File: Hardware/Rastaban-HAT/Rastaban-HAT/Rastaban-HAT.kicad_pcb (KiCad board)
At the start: 2 copper layers, 99.1 x 99.7 mm, 129 parts, among them IC1 BCR420UW6-7, IC2 BCM53DS, J1 1778780, J10 GPIO, J11 Conn_01x06_Male, J12 Conn_01x03_Male, J13 Conn_01x03_Male, J2 1778780, J3 1778780, J4 Screw_Terminal_01x02, J5 Jack-DC 12V+, J6 SM04B-SRSS-TB(LF)(SN), J7 Screw_Terminal_01x02, J8 Screw_Terminal_01x02, J9 Conn_01x05_Male, M1 Fan, Q1 PMV15ENE, Q2 PMV15ENE, Q3 DMG2305UX-7, Q4 PMV15ENE, Q5 PMV15ENE, Q6 2N70002HWX, U1 DRV8870DDA, U10 xl6009_module, U2 TLV1117-33, U3 TMC2208_Carrier, U4 TMC2208_Carrier, U5 RT7272AGSP, U6 TMC2208_Carrier, U7 DRV8838 POLOLU, U8 TLV1117-33, U9 CAT24C256

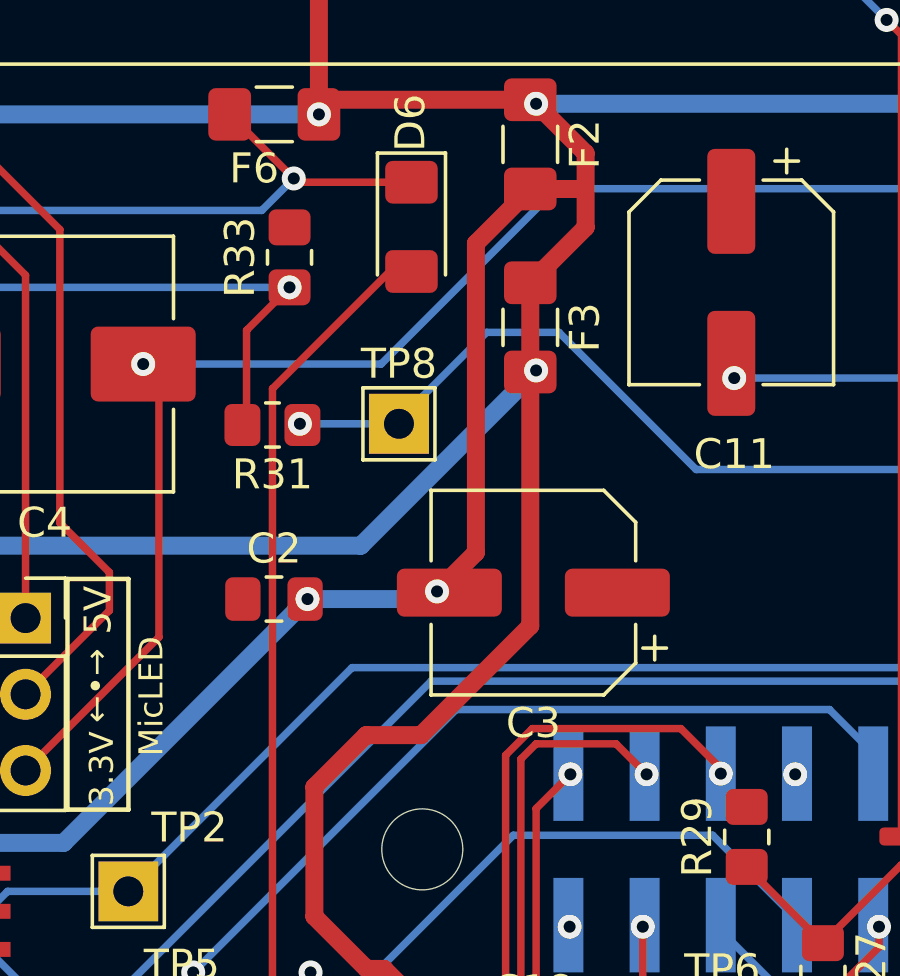
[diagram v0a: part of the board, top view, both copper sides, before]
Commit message: fixed parity problem ERC: 0 err 0 war
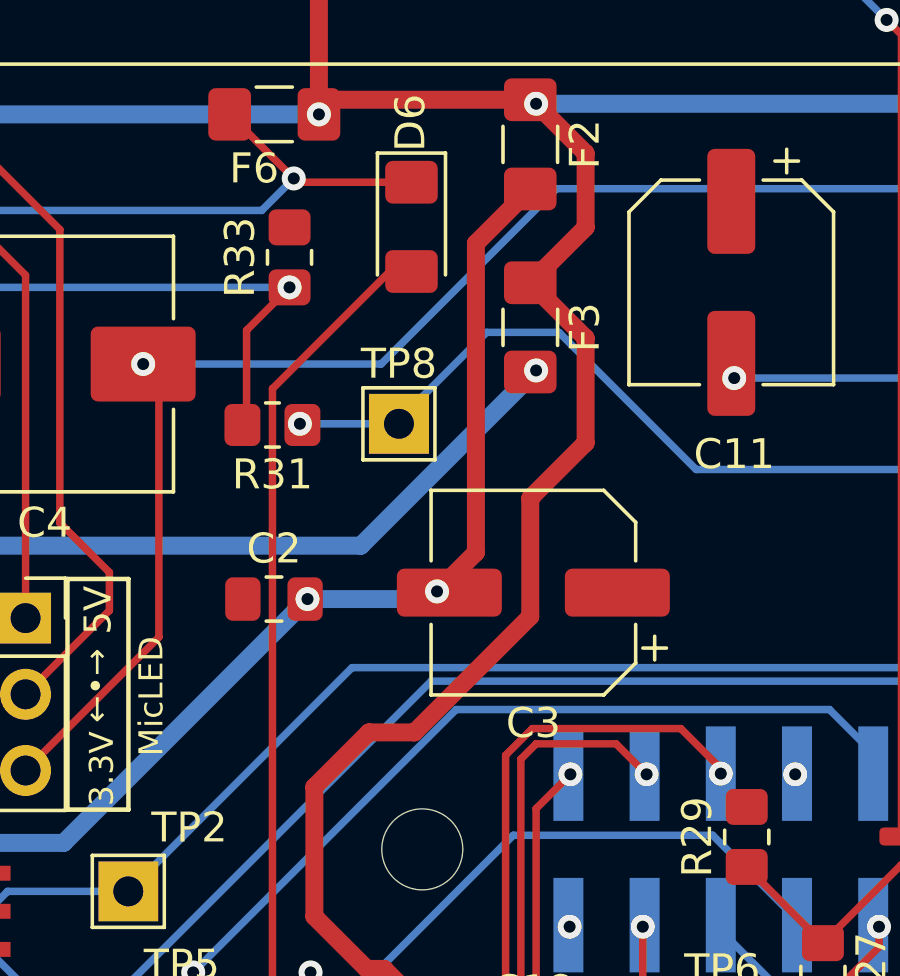
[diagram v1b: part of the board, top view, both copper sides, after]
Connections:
- C18 pad 1: Net-(C2-Pad2) -> 12V+
- C6 pad 1: Net-(C2-Pad2) -> 12V+
- C7 pad 1: Net-(C2-Pad2) -> 12V+
- C8 pad 1: Net-(C2-Pad2) -> 12V+
- F1 pad 1: Net-(C2-Pad2) -> 12V+
- F2 pad 1: Net-(C2-Pad2) -> 12V+
- F3 pad 1: Net-(C2-Pad2) -> 12V+
- F3 pad 2: Net-(C2-Pad2) -> Net-(F3-Pad2)
- F5 pad 1: Net-(C2-Pad2) -> 12V+
- F6 pad 1: Net-(C2-Pad2) -> 12V+
- FB1 pad 2: Net-(C2-Pad2) -> 12V+
- JP2 pad 3: Net-(C2-Pad2) -> 12V+
- JP3 pad 3: Net-(C2-Pad2) -> 12V+
- R10 pad 1: Net-(C2-Pad2) -> 12V+
- R3 pad 2: Net-(C2-Pad2) -> Net-(F3-Pad2)
- U10 pad 1: Net-(C2-Pad2) -> 12V+
- U5 pad 8: Net-(C2-Pad2) -> 12V+
- U6 pad JP2_1: Net-(C2-Pad2) -> 12V+
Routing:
- net Net-(C2-Pad2): track 324.9 -> 39.6 mm, vias 14 -> 3
- net 12V+: track 0.00 -> 251.4 mm, vias 0 -> 9
- net Net-(F3-Pad2): track 0.00 -> 33.4 mm, vias 0 -> 2

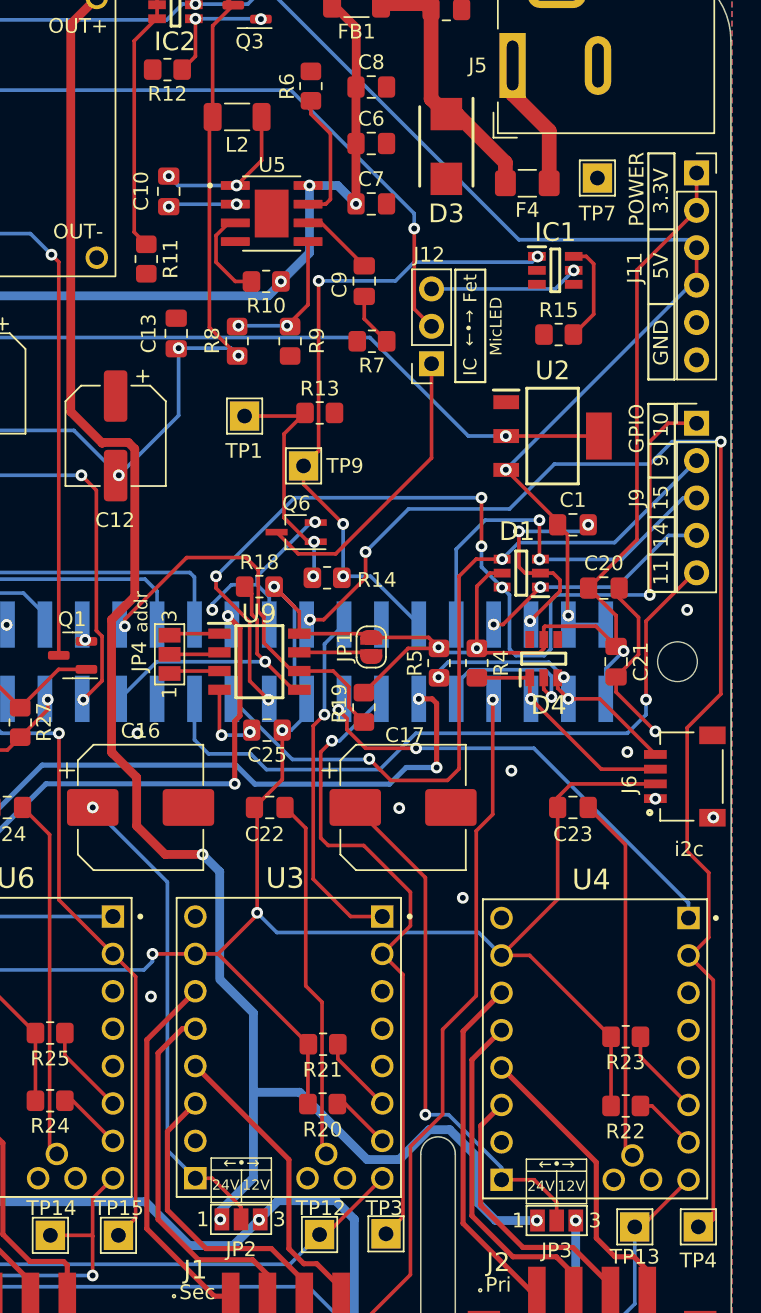
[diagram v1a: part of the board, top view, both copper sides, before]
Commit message: increased width stepper trace and rerun drc 0,0
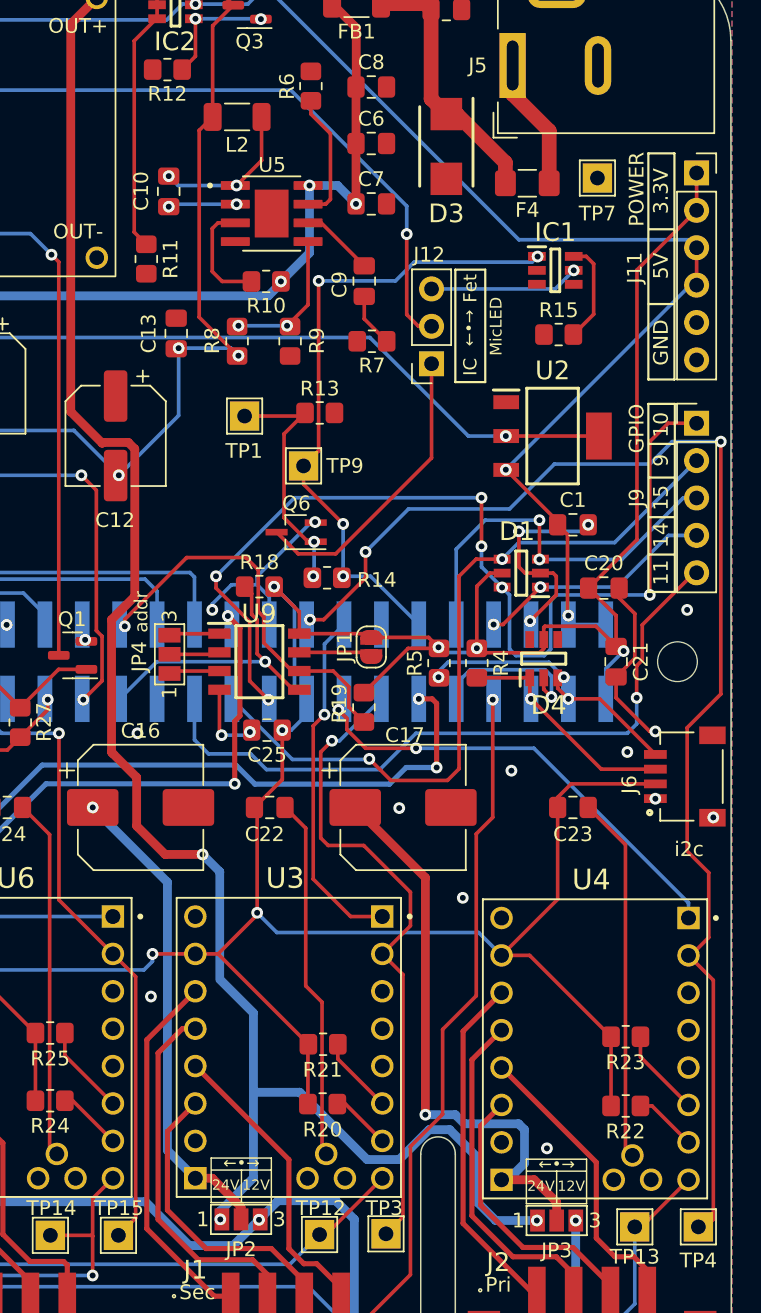
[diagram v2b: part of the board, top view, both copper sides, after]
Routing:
- net Net-(C17-Pad1): track 35.9 -> 39.9 mm
- net Net-(R10-Pad2): track 6.43 -> 7.59 mm
- net Net-(C11-Pad2): track 53.8 -> 54.4 mm
- net Net-(D2-PadK): track 79.2 -> 79.7 mm
- net GND: track 55.4 -> 55.2 mm, vias 24 -> 25

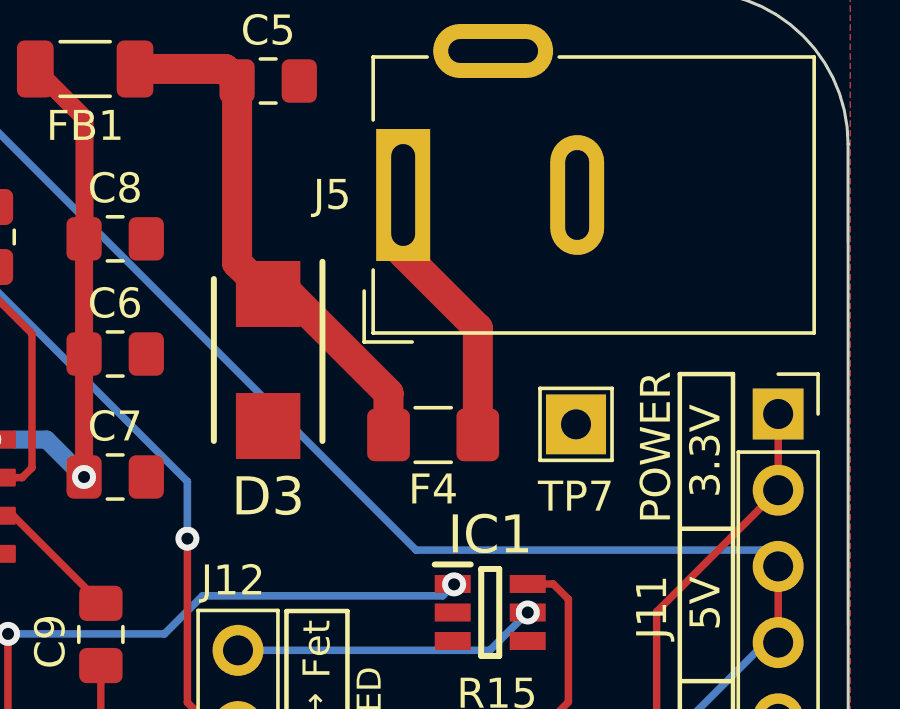
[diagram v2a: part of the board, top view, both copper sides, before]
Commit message: removed useless testpoint (GND)
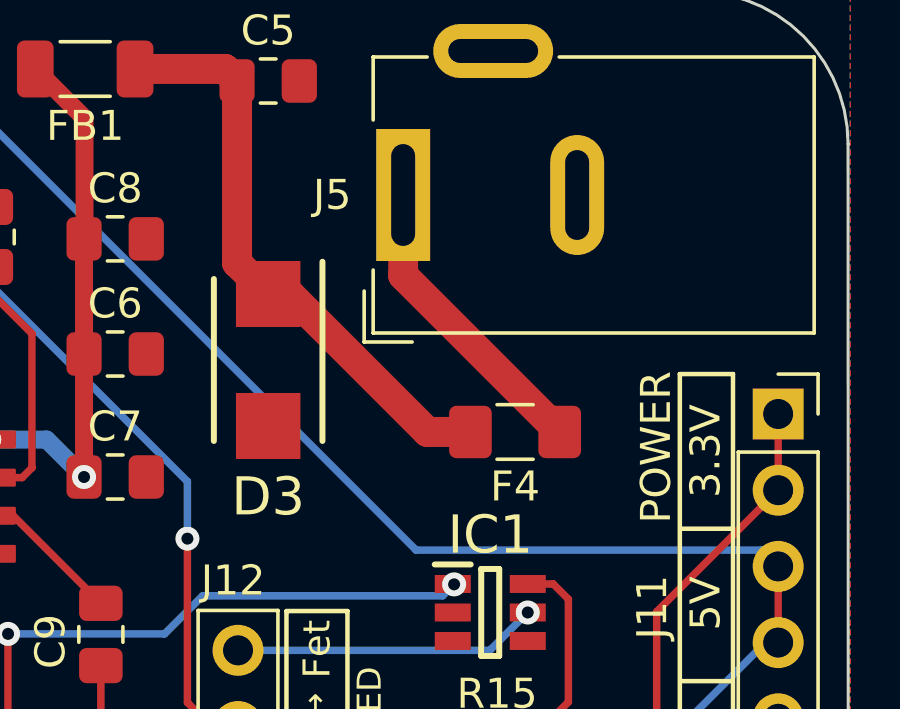
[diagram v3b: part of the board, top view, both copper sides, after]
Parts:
- removed TP7: TestPoint, TestPoint:TestPoint_THTPad_2.0x2.0mm_Drill1.0mm
- moved F4 2.73 mm to (240.5, 125.9)
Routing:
- net Net-(C5-Pad1): track 17.9 -> 19.7 mm
- net 12VIN: track 9.03 -> 10.1 mm
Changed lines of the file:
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@@
   )
   (footprint "Fuse:Fuse_1206_3216Metric_Pad1.42x1.75mm_HandSolder" (layer "F.Cu")
-    (at 237.808 125.958 180)
+    (at 240.538 125.857 180)
     (descr "Fuse SMD 1206 (3216 Metric), square (rectangular) end terminal, IPC_7351 nominal with elongated pad for handsoldering. (Body size source: http://www.tortai-tech.com/upload/download/2011102023233369053.pdf), generated with kicad-footprint-generator")
     (tags "fuse handsolder")
@@
     )
   )
-  (footprint "TestPoint:TestPoint_THTPad_2.0x2.0mm_Drill1.0mm" (layer "F.Cu")
-    (at 242.57 125.603)
-    (descr "THT rectangular pad as test Point, square 2.0mm_Drill1.0mm  side length, hole diameter 1.0mm")
-    (tags "test point THT pad rectangle square")
-    (property "LCSC" "x")
-    (property "Mouser" "x")
-    (property "Sheetfile" "Rastaban-HAT.kicad_sch")
-    (property "Sheetname" "")
-    (attr exclude_from_pos_files)
-    (fp_text reference "TP7" (at 0 2.413) (layer "F.SilkS")
-      (effects (font (size 1 1) (thickness 0.15)))
-    )
-    (fp_text value "TestPoint" (at 0 3.048) (layer "F.Fab")
-      (effects (font (size 1 1) (thickness 0.15)))
-    )
-    (fp_text user "${REFERENCE}" (at 0 -2) (layer "F.Fab")
-      (effects (font (size 1 1) (thickness 0.15)))
-    )
-    (fp_line (start 1.2 1.2) (end -1.2 1.2) (layer "F.SilkS") (width 0.12))
-    (fp_line (start 1.2 -1.2) (end 1.2 1.2) (layer "F.SilkS") (width 0.12))
-    (fp_line (start -1.2 -1.2) (end 1.2 -1.2) (layer "F.SilkS") (width 0.12))
-    (fp_line (start -1.2 1.2) (end -1.2 -1.2) (layer "F.SilkS") (width 0.12))
-    (fp_line (start -1.5 -1.5) (end -1.5 1.5) (layer "F.CrtYd") (width 0.05))
-    (fp_line (start -1.5 -1.5) (end 1.5 -1.5) (layer "F.CrtYd") (width 0.05))
-    (fp_line (start 1.5 1.5) (end -1.5 1.5) (layer "F.CrtYd") (width 0.05))
-    (fp_line (start 1.5 1.5) (end 1.5 -1.5) (layer "F.CrtYd") (width 0.05))
-    (pad "1" thru_hole rect (at 0 0) (size 2 2) (drill 1) (layers *.Cu *.Mask)
-      (net 1 "GND") (pinfunction "1") (pintype "passive"))
-  )
   (footprint "Package_TO_SOT_SMD:SOT-23" (layer "F.Cu")
     (at 167.308 167.458 90)
@@
   (segment (start 170.307 158.242) (end 178.054 158.242) (width 0.6) (layer "B.Cu") (net 3))
   (segment (start 227.8719 113.7566) (end 230.8691 113.7566) (width 1) (layer "F.Cu") (net 4))
+  (segment (start 232.308 121.258) (end 233.018 121.258) (width 1) (layer "F.Cu") (net 4))
   (segment (start 231.2705 114.158) (end 231.2705 120.2205) (width 1) (layer "F.Cu") (net 4))
   (segment (start 230.8691 113.7566) (end 231.2705 114.158) (width 1) (layer "F.Cu") (net 4))
-  (segment (start 232.308 121.258) (end 233.018 121.258) (width 1) (layer "F.Cu") (net 4))
-  (segment (start 236.3205 124.5605) (end 236.3205 125.958) (width 1) (layer "F.Cu") (net 4))
+  (segment (start 237.617 125.857) (end 239.0505 125.857) (width 1) (layer "F.Cu") (net 4))
+  (segment (start 233.018 121.258) (end 237.617 125.857) (width 1) (layer "F.Cu") (net 4))
   (segment (start 231.2705 120.2205) (end 232.308 121.258) (width 1) (layer "F.Cu") (net 4))
-  (segment (start 233.018 121.258) (end 236.3205 124.5605) (width 1) (layer "F.Cu") (net 4))
   (segment (start 227.8705 113.758) (end 227.8719 113.7566) (width 1) (layer "F.Cu") (net 4))
   (segment (start 226.731 135.168) (end 228.255 136.692) (width 0.25) (layer "F.Cu") (net 5))
@@
   (segment (start 167.6765 133.3865) (end 167.6765 134.366) (width 0.25) (layer "F.Cu") (net 11))
   (segment (start 162.376 131.507333) (end 165.797333 131.507333) (width 0.25) (layer "F.Cu") (net 11))
-  (segment (start 239.2955 122.3947) (end 236.808 119.9072) (width 1) (layer "F.Cu") (net 12))
-  (segment (start 236.808 119.9072) (end 236.808 117.958) (width 1) (layer "F.Cu") (net 12))
-  (segment (start 239.2955 125.958) (end 239.2955 122.3947) (width 1) (layer "F.Cu") (net 12))
+  (segment (start 242.0255 125.857) (end 236.808 120.6395) (width 1) (layer "F.Cu") (net 12))
+  (segment (start 236.808 120.6395) (end 236.808 117.958) (width 1) (layer "F.Cu") (net 12))
   (segment (start 240.598 160.983) (end 242.733 160.983) (width 0.25) (layer "F.Cu") (net 13))
   (segment (start 239.873 160.258) (end 240.598 160.983) (width 0.25) (layer "F.Cu") (net 13))

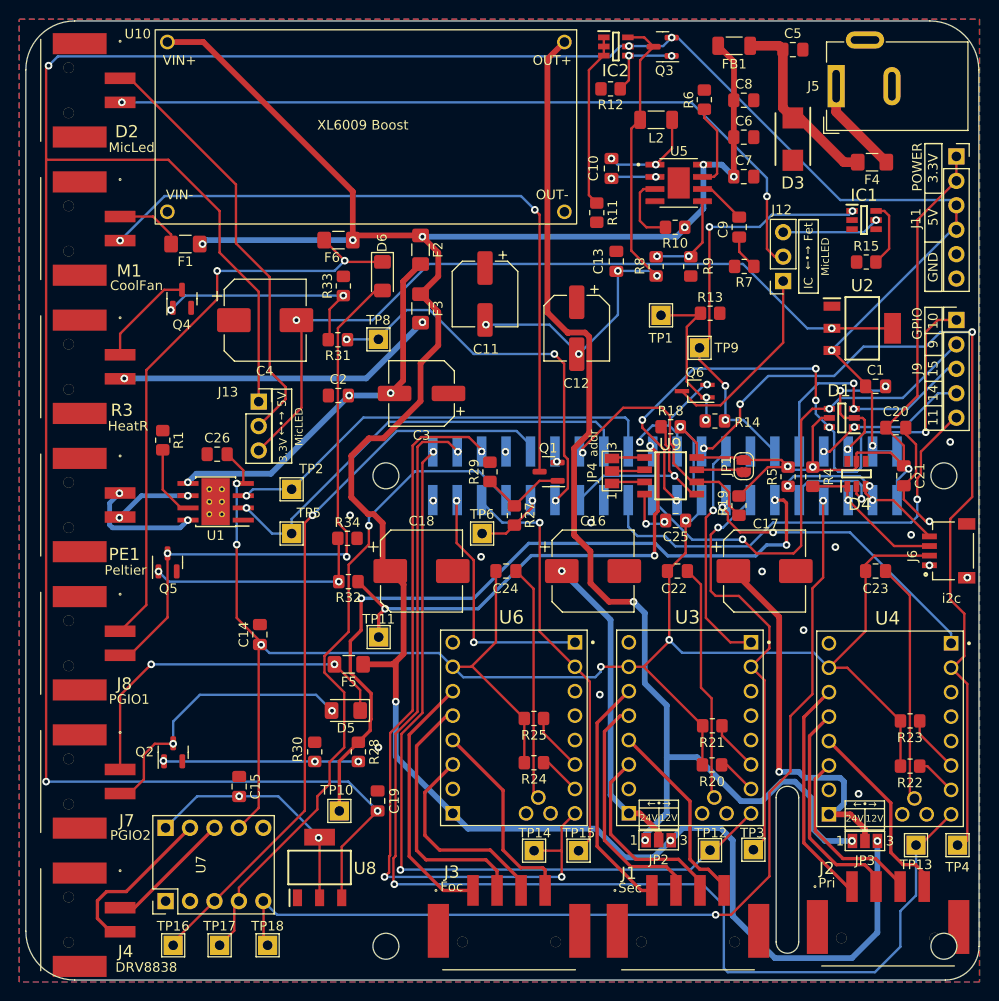
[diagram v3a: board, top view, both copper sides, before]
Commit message: improved wiring
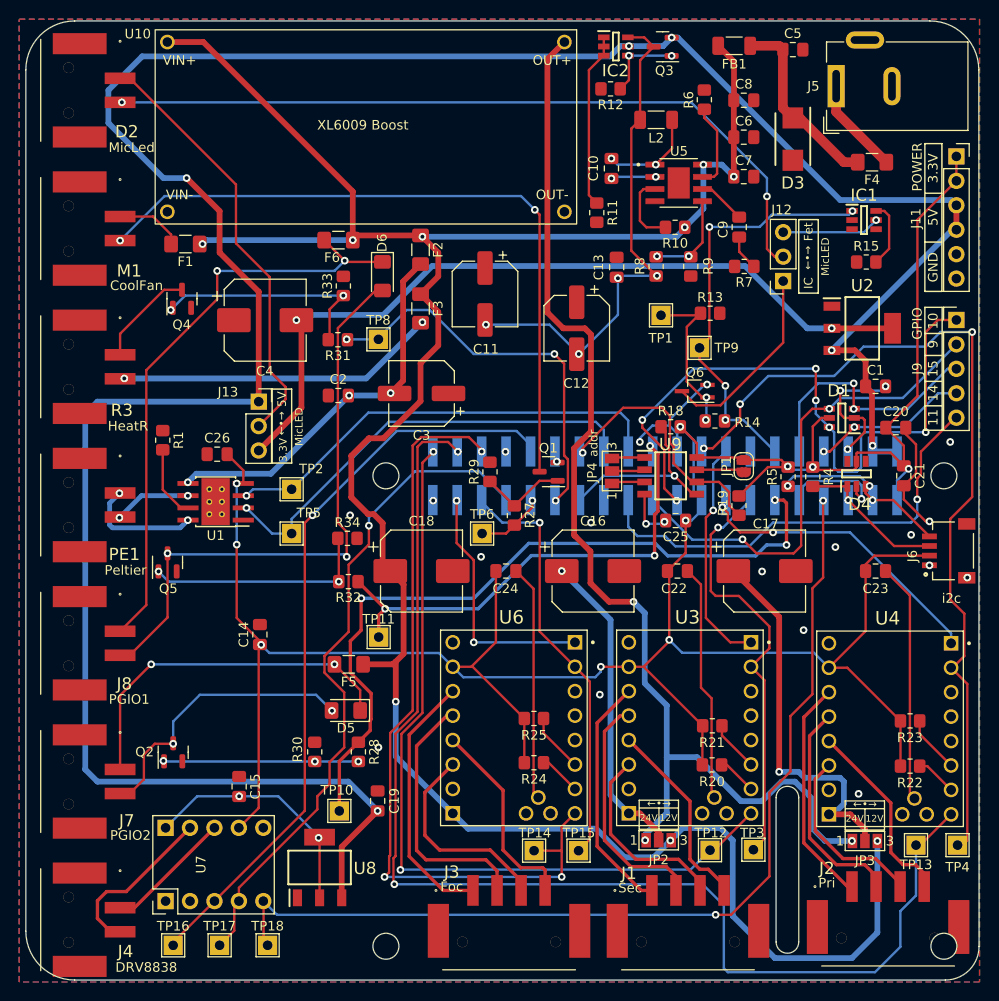
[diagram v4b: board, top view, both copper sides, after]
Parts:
- moved C13 0.62 mm to (214.0, 136.8)
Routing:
- net 5V+: track 300.3 -> 272.5 mm, vias 7 -> 6
- net Net-(C11-Pad2): track 54.4 -> 53.5 mm

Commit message: added silkscreen on back
added useful board information
added logo to files
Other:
- board text added: "Project: Rastaban Version: 0.1 Date: 31-10-2022 Designed by: Casper R. Tak"
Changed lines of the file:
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@@
   (gr_line locked (start 251.638002 116.255998) (end 251.6632 207.3656) (layer "Edge.Cuts") (width 0.1))
   (gr_arc locked (start 251.6632 207.3656) (mid 250.636551 209.844151) (end 248.158 210.8708) (layer "Edge.Cuts") (width 0.1))
+  (gr_text "Project: Rastaban\nVersion: 0.1\nDate: 31-10-2022\nDesigned by: Casper R. Tak\n " (at 239.395 205.613) (layer "B.SilkS")
+    (effects (font (size 2 2) (thickness 0.25)) (justify left mirror))
+  )
   (gr_text "12V" (at 219.3798 194.0052) (layer "F.SilkS")
     (effects (font (size 0.7 0.7) (thickness 0.15)))

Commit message: Added logo to silkscreen back
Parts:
- added G***: LOGO, LOGO, B.Cu at (205.5, 160.1)
